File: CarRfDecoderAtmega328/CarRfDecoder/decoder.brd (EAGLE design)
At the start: 98.7 x 80 mm, 52 parts, among them T1 BC847, T2 BC847, T3 IRLML6402, U2 RFM69CW, U3 MCP73831, U4 ATMEGA328P, U6 MIC5219 3.3V, Y1 16MHZ

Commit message: bug fixes and better board routing
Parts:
- removed SS: (no value), wirepad:SMD1,27-2,54
- moved AUX3 17.3 mm to (15.7, 0.91)
- moved AUX4 17.3 mm to (17.6, 0.93)
- moved AUX2 17.3 mm to (13.8, 0.92)
- moved AUX1 17.3 mm to (12.0, 0.94)
- moved R9 10.7 mm to (13.3, 3.55), turned to 180 degrees
- moved SI 9.75 mm to (18.7, 17.5)
- moved SCK 7.94 mm to (16.8, 17.5)
- moved SER_V+ 6.53 mm to (10.2, 0.92)
- moved SER_DTR 6.33 mm to (8.40, 0.92)
- moved C1 6.19 mm to (5.92, 0.83)
- moved R1 5.87 mm to (3.02, 0.74)
- moved LIGHT 3.41 mm to (11.5, 17.4)
- moved SER_TX 3.35 mm to (23.8, 0.91)
- moved SER_RX 3.33 mm to (25.6, 0.90)
- moved GND 2.41 mm to (28.3, 2.72), turned to 90 degrees
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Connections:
- removed net AX1: R9.1, U4.25
- removed net AX2: R9.2, U4.22
- removed net AX3: R9.3, U4.19
- removed net AX4: R9.4, U4.10
- removed net N$24: AUX4.1, R9.5
- new net A2: R9.4, U4.25
- new net A6: C4.1, R6.3, R6.4, U4.19
- new net A7: R4.1, R5.2, U4.22
- new net D6: R9.2, U4.10
- new net M: AUX1.1, R9.5
- net A1: now also U3.1; no longer R11.1
- net A3: now also R9.3; no longer C4.1, R6.3, R6.4
- net A5: now also R9.1; no longer R4.1, R5.2
- net D7: now also R11.1; no longer U3.1
- net N$21: now also AUX4.1; no longer AUX1.1
- net N$22: now also AUX3.1; no longer AUX2.1
- net N$23: now also AUX2.1; no longer AUX3.1
- net SS: no longer SS.1
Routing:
- net GND: track 108.4 -> 126.9 mm, vias 9 -> 8
- net A7: track 0.00 -> 18.0 mm, vias 0 -> 1
- net BAT+: track 68.7 -> 52.0 mm, vias 7 -> 8
- net D6: track 0.00 -> 15.7 mm, vias 0 -> 4
- net D7: track 25.4 -> 10.0 mm
- net A5: track 19.9 -> 5.30 mm, vias 2 -> 0
- net AX1: track 12.5 -> 0.00 mm, vias 2 -> 0
- net A3: track 16.9 -> 5.52 mm, vias 2 -> 0
- net A6: track 0.00 -> 9.77 mm, vias 0 -> 1
- net SS: track 22.0 -> 12.5 mm, vias 2 -> 1
- net N$24: track 8.73 -> 0.00 mm
- net BL: track 6.59 -> 15.2 mm, vias 2 -> 0
- net AX4: track 8.59 -> 0.00 mm
- net SCK: track 27.8 -> 19.8 mm, vias 2 -> 1
- net AX2: track 7.52 -> 0.00 mm
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
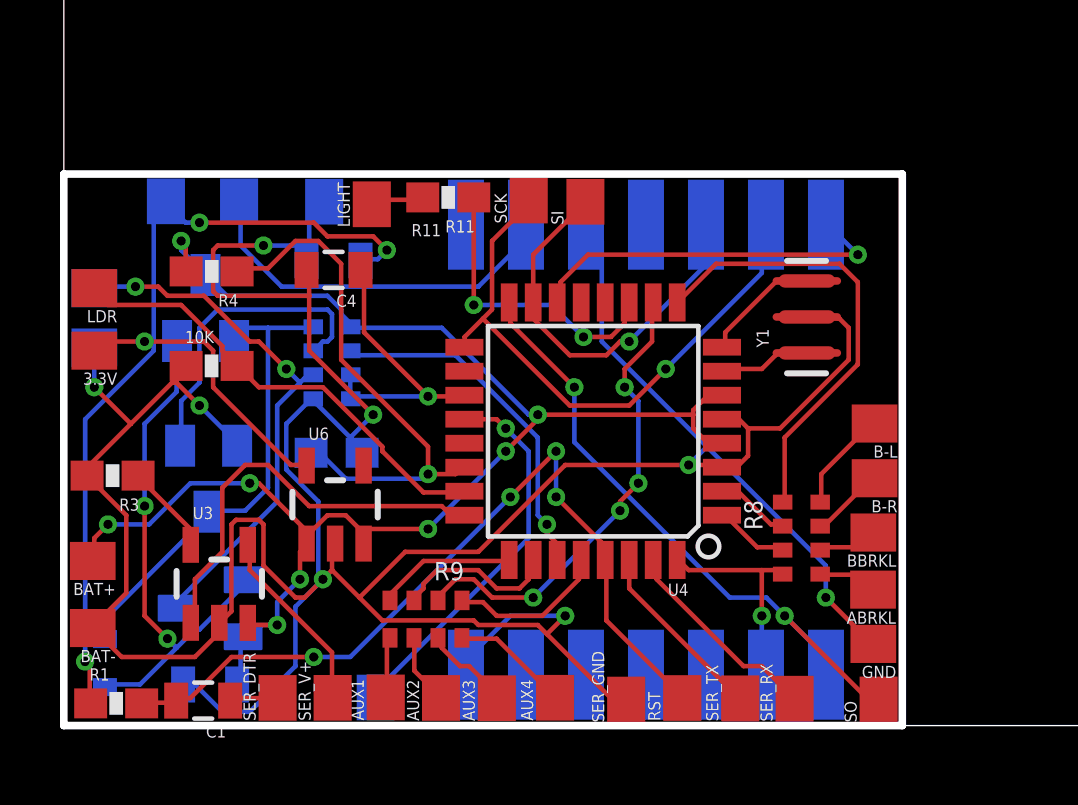
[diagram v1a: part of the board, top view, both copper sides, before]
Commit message: Fix light board. Fix carsystem board.
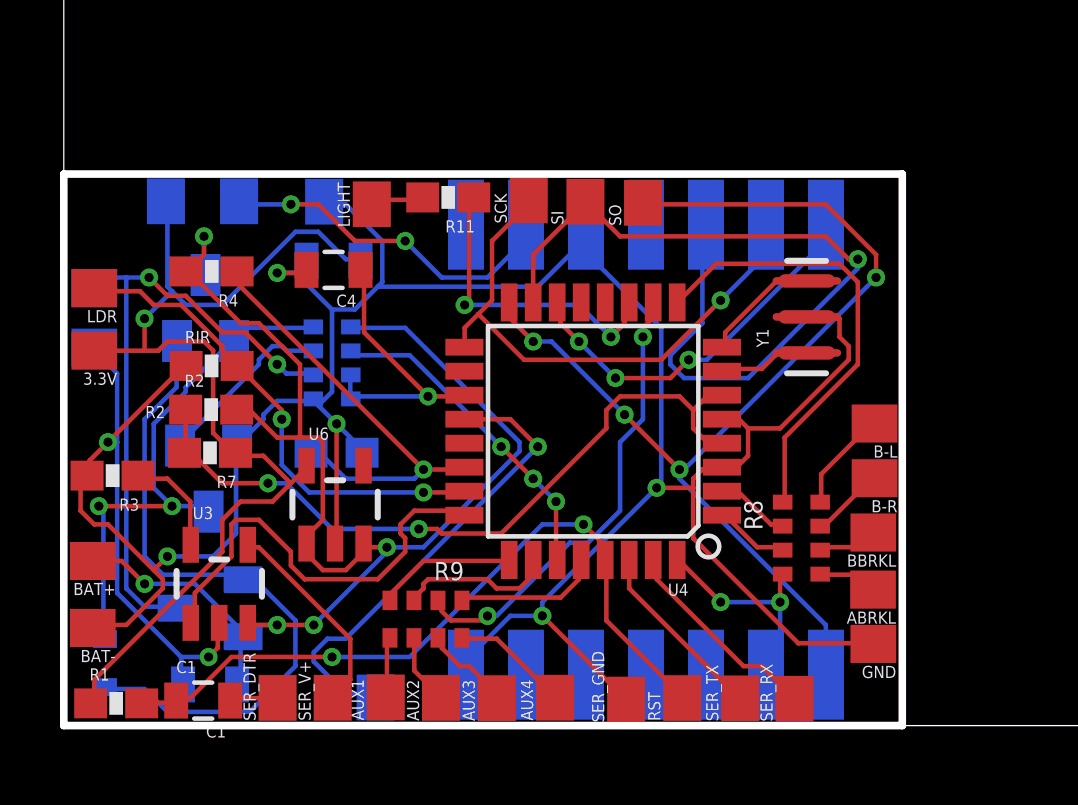
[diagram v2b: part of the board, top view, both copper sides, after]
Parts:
- added R2, R7: 0, SparkFun-Resistors:0603-RES
- moved SO 18.3 mm to (20.6, 17.4)
- renumbered 10K to RIR
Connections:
- new net N$6: R2.1, R7.2, U4.4, U4.6
- net BAT+: now also R2.2; no longer U4.4, U4.6
- net VCC: now also R7.1
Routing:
- net N$6: track 0.00 -> 24.9 mm, vias 0 -> 2
- net GND: track 126.9 -> 111.4 mm, vias 8 -> 7
- net MOSI: track 13.5 -> 27.4 mm
- net MISO: track 21.8 -> 35.6 mm, vias 2 -> 4
- net N$14: track 17.4 -> 22.4 mm, vias 2 -> 0
- net N$17: track 10.5 -> 6.01 mm
- net A7: track 18.0 -> 14.8 mm
- net N$15: track 18.0 -> 21.2 mm
- net AREF: track 13.0 -> 16.0 mm
- net N$5: track 27.3 -> 24.4 mm, vias 4 -> 2
- net BAT+: track 52.0 -> 49.5 mm, vias 8 -> 5
- net N$19: track 16.2 -> 18.0 mm, vias 0 -> 2
- net VCC: track 36.9 -> 35.2 mm, vias 4 -> 1
- net SCK: track 19.8 -> 18.5 mm
- net N$1: track 12.7 -> 11.6 mm, vias 0 -> 2
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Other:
- board text added: "C1"
- board text added: "R2"
- board text removed: "R11"

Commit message: CAM file for boards.
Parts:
- renumbered R2 to R_BAT, R7 to R_3.3V
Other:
- board text added: "R-BAT"
- board text removed: "R2"
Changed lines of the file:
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@@
 <layer number="20" name="Dimension" color="15" fill="1" visible="yes" active="yes"/>
 <layer number="21" name="tPlace" color="7" fill="1" visible="yes" active="yes"/>
-<layer number="22" name="bPlace" color="7" fill="1" visible="no" active="yes"/>
+<layer number="22" name="bPlace" color="7" fill="1" visible="yes" active="yes"/>
 <layer number="23" name="tOrigins" color="15" fill="1" visible="yes" active="yes"/>
 <layer number="24" name="bOrigins" color="15" fill="1" visible="yes" active="yes"/>
 <layer number="25" name="tNames" color="7" fill="1" visible="yes" active="yes"/>
-<layer number="26" name="bNames" color="7" fill="1" visible="no" active="yes"/>
+<layer number="26" name="bNames" color="7" fill="1" visible="yes" active="yes"/>
 <layer number="27" name="tValues" color="7" fill="1" visible="no" active="yes"/>
 <layer number="28" name="bValues" color="7" fill="1" visible="no" active="yes"/>
@@
 <layer number="116" name="Patch_BOT" color="9" fill="4" visible="no" active="yes"/>
 <layer number="121" name="_tsilk" color="7" fill="1" visible="yes" active="yes"/>
-<layer number="122" name="_bsilk" color="7" fill="1" visible="no" active="yes"/>
+<layer number="122" name="_bsilk" color="7" fill="1" visible="yes" active="yes"/>
 <layer number="123" name="tTestmark" color="7" fill="1" visible="no" active="yes"/>
 <layer number="124" name="bTestmark" color="7" fill="1" visible="no" active="yes"/>
@@
 <wire x1="29.21931875" y1="0" x2="1.27" y2="0" width="0.254" layer="20"/>
 <wire x1="1.27" y1="0" x2="1.27" y2="18.383696875" width="0.254" layer="20"/>
-<text x="13.6652" y="0.5588" size="0.4064" layer="122" rot="MR0">gnd</text>
+<text x="13.925321875" y="0.506771875" size="0.4064" layer="122" rot="MR0">gnd</text>
 <text x="17.526" y="17.2212" size="0.4064" layer="122" rot="MR90">3.3</text>
 <text x="27.2796" y="18.034" size="0.4064" layer="122" rot="MR180">hss</text>
@@
 <text x="23.4696" y="18.034" size="0.4064" layer="122" ratio="7" rot="MR180">si</text>
 <text x="19.6088" y="17.2212" size="0.4064" layer="122" rot="MR90">gnd</text>
-<text x="15.8496" y="0.3556" size="0.4064" layer="122" rot="MR90">rst</text>
+<text x="15.706534375" y="0.316575" size="0.4064" layer="122" rot="MR90">rst</text>
 <text x="5.0185" y="1.748625" size="0.4064" layer="121">C1</text>
-<text x="3.98438125" y="10.246528125" size="0.4064" layer="121">R2</text>
+<text x="2.959125" y="10.246528125" size="0.4064" layer="121">R-BAT</text>
 </plain>
 <attributes>
@@
 <element name="C1" library="SparkFun-Capacitors" package="0805" value="1uF" x="5.916221875" y="0.832240625" rot="R180"/>
 <element name="RST" library="wirepad" package="SMD1,27-2,54" value="" x="21.885759375" y="0.91805"/>
-<element name="R2" library="SparkFun-Resistors" package="0603-RES" value="0" x="6.18259375" y="10.53095625"/>
-<element name="R7" library="SparkFun-Resistors" package="0603-RES" value="0" x="6.143734375" y="9.091575" rot="R180"/>
+<element name="R_BAT" library="SparkFun-Resistors" package="0603-RES" value="0" x="6.18259375" y="10.53095625"/>
+<element name="R_3.3V" library="SparkFun-Resistors" package="0603-RES" value="0" x="6.143734375" y="9.091575" rot="R180"/>
 </elements>
 <signals>
@@
 <contactref element="VJ1" pad="1"/>
 <contactref element="C3" pad="2"/>
-<contactref element="R7" pad="1"/>
+<contactref element="R_3.3V" pad="1"/>
 <wire x1="10.668" y1="15.5448" x2="11.1252" y2="15.5448" width="0.1524" layer="16"/>
 <wire x1="9.7536" y1="16.4592" x2="10.668" y2="15.5448" width="0.1524" layer="16"/>
@@
 <contactref element="T3" pad="2"/>
 <contactref element="T1" pad="3"/>
-<contactref element="R2" pad="2"/>
+<contactref element="R_BAT" pad="2"/>
 <wire x1="7.4676" y1="10.5156" x2="7.1628" y2="10.5156" width="0.1524" layer="1"/>
 <wire x1="8.382" y1="9.6012" x2="7.4676" y2="10.5156" width="0.1524" layer="1"/>
@@
 <contactref element="U4" pad="6"/>
 <contactref element="U4" pad="4"/>
-<contactref element="R2" pad="1"/>
-<contactref element="R7" pad="2"/>
+<contactref element="R_BAT" pad="1"/>
+<contactref element="R_3.3V" pad="2"/>
 <wire x1="5.334" y1="10.5156" x2="5.334" y2="9.144" width="0.1524" layer="1"/>
 <wire x1="5.334" y1="9.144" x2="5.293734375" y2="9.091575" width="0.1524" layer="1"/>

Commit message: small fixes for vcc.
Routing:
- net GND: track 111.4 -> 0.00 mm, vias 7 -> 0
- net BAT+: track 49.5 -> 0.00 mm, vias 5 -> 0
- net MISO: track 35.6 -> 0.00 mm, vias 4 -> 0
- net VCC: track 35.2 -> 0.00 mm, vias 1 -> 0
- net MOSI: track 27.4 -> 0.00 mm, vias 1 -> 0
- net N$6: track 24.9 -> 0.00 mm, vias 2 -> 0
- net N$5: track 24.4 -> 0.00 mm, vias 2 -> 0
- net N$14: track 22.4 -> 0.00 mm
- net N$15: track 21.2 -> 0.00 mm, vias 2 -> 0
- net SCK: track 18.5 -> 0.00 mm, vias 1 -> 0
- net N$19: track 18.0 -> 0.00 mm, vias 2 -> 0
- net A0: track 16.4 -> 0.00 mm, vias 2 -> 0
- net AREF: track 16.0 -> 0.00 mm, vias 1 -> 0
- net D6: track 15.4 -> 0.00 mm, vias 2 -> 0
- net BL: track 15.2 -> 0.00 mm
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
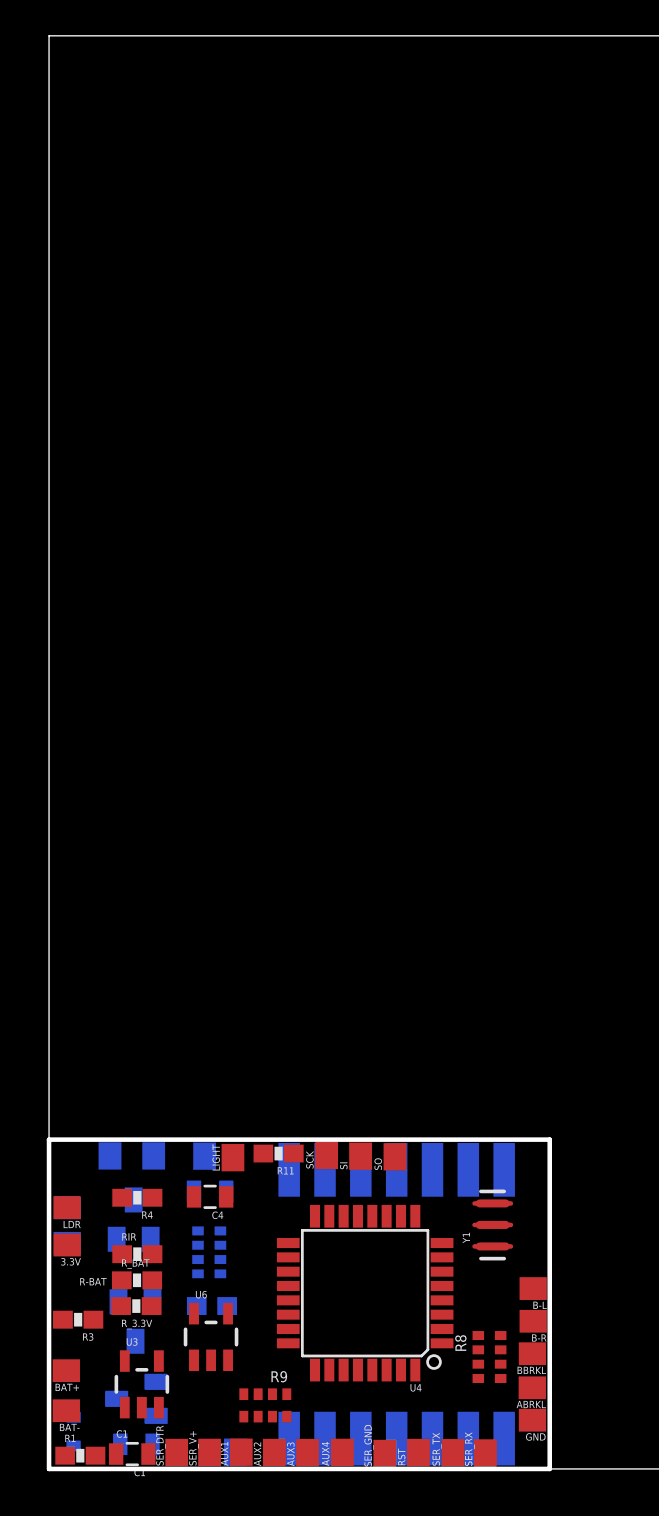
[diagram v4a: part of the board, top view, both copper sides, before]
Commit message: Change the pin to H-bridge to allow reverse control of the motor using A5
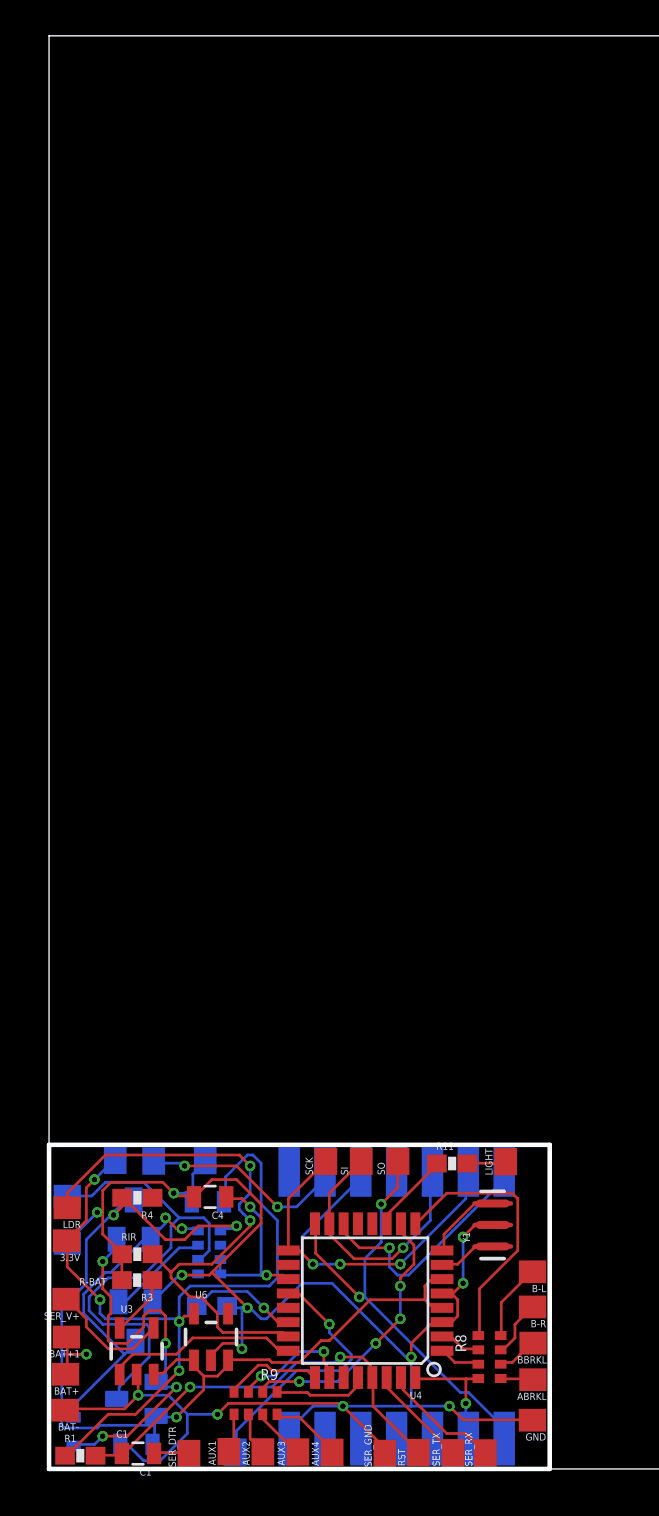
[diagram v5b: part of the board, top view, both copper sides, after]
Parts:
- removed R_3.3V, R_BAT: 0, SparkFun-Resistors:0603-RES
- added BAT+1: (no value), wirepad:SMD1,27-2,54
- moved LIGHT 15.2 mm to (26.8, 17.2)
- moved SER_V+ 11.7 mm to (2.22, 9.47), turned to 90 degrees
- moved R11 9.70 mm to (23.8, 17.0), turned to 0 degrees
- moved R3 3.97 mm to (6.19, 10.5)
- moved U3 1.87 mm to (6.16, 6.57)
- moved B-L 0.94 mm to (28.3, 11.0)
- moved B-R 0.80 mm to (28.3, 9.04)
- moved AUX1 0.69 mm to (11.3, 0.97)
- moved SER_DTR 0.69 mm to (9.08, 0.86)
- moved MOTOR 0.65 mm to (2.29, 15.2)
- moved AUX2 0.64 mm to (13.2, 0.95)
- moved C3 0.60 mm to (10.1, 14.9)
- moved BBRKL 0.59 mm to (28.3, 7.02)
- moved AUX4 0.57 mm to (17.1, 0.93)
- moved R9 0.56 mm to (12.8, 3.67)
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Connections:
- removed net N$6: R_3.3V.2, R_BAT.1, U4.4, U4.6
- net BAT+: now also BAT+1.1, U4.4, U4.6; no longer R_BAT.2
- net VCC: no longer R_3.3V.1
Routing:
- net GND: track 0.00 -> 116.7 mm, vias 0 -> 12
- net BAT+: track 0.00 -> 61.7 mm, vias 0 -> 4
- net VCC: track 0.00 -> 45.3 mm, vias 0 -> 4
- net A0: track 0.00 -> 31.6 mm, vias 0 -> 2
- net N$15: track 0.00 -> 28.4 mm
- net MISO: track 0.00 -> 25.1 mm, vias 0 -> 2
- net N$5: track 0.00 -> 23.8 mm, vias 0 -> 2
- net N$14: track 0.00 -> 23.7 mm, vias 0 -> 4
- net SCK: track 0.00 -> 19.3 mm, vias 0 -> 3
- net N$19: track 0.00 -> 18.7 mm, vias 0 -> 2
- net D6: track 0.00 -> 15.4 mm, vias 0 -> 4
- net BL: track 0.00 -> 15.1 mm
- net MOSI: track 0.00 -> 14.8 mm, vias 0 -> 1
- net AREF: track 0.00 -> 14.8 mm, vias 0 -> 1
- net SS: track 0.00 -> 13.8 mm, vias 0 -> 1
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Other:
- outline, holes or cut-outs redrawn

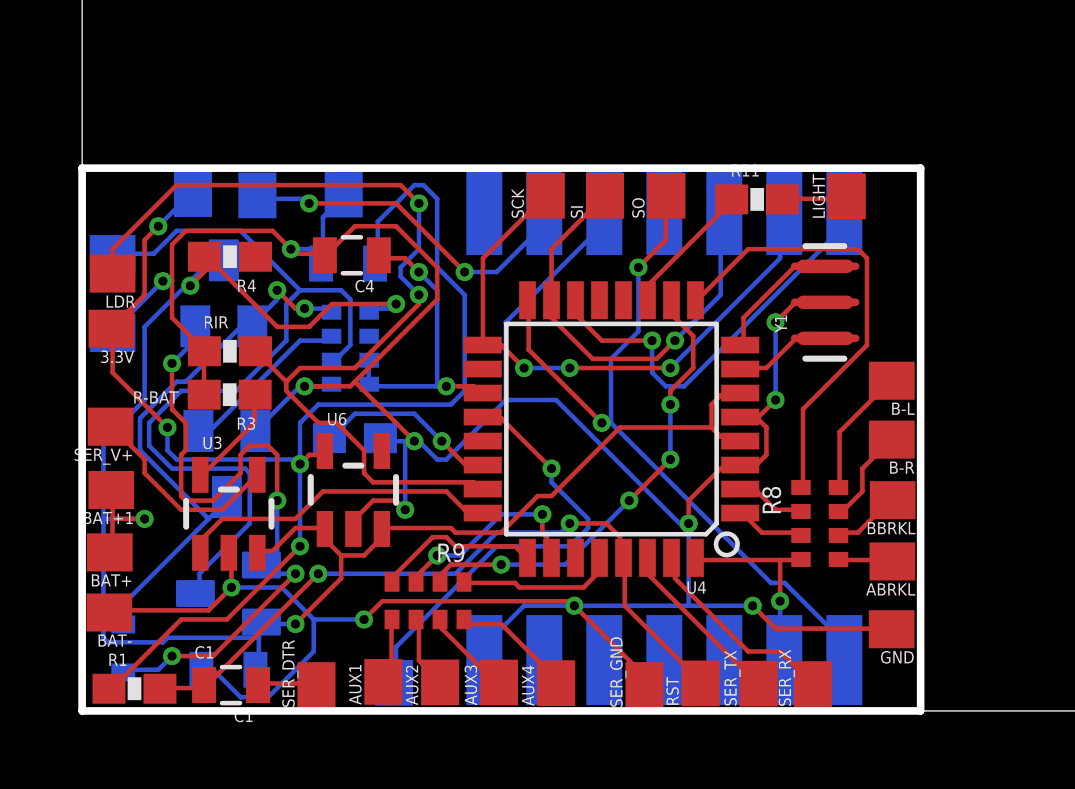
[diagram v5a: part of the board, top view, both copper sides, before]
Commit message: New layout for RFM69HC
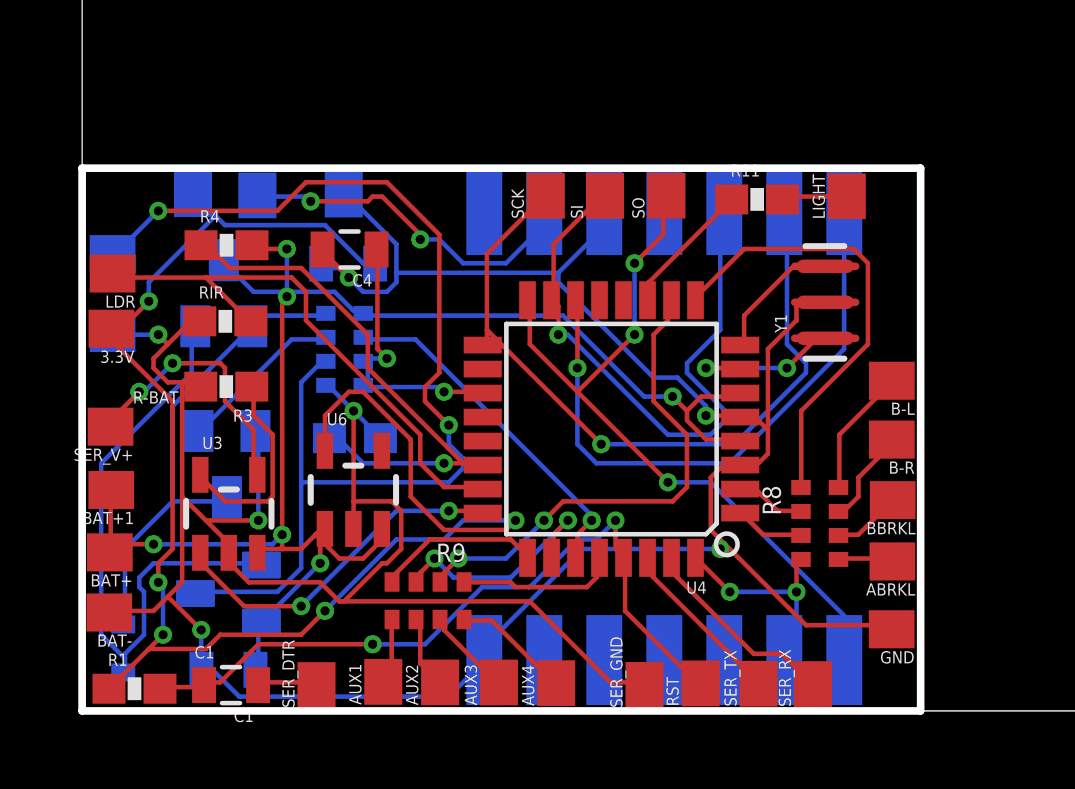
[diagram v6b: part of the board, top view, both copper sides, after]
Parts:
- removed 2.56V: (no value), wirepad:SMD1,27-2,54
- moved RIR 1.01 mm to (6.04, 13.0)
- moved R4 0.40 mm to (6.08, 15.5), turned to 0 degrees
- moved R3 0.29 mm to (6.08, 10.8)
- moved C4 0.21 mm to (10.2, 15.4)
- moved R6 0.20 mm to (10.0, 12.1)
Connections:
- net AREF: no longer 2.56V.1
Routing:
- net AREF: track 14.8 -> 0.00 mm, vias 1 -> 0
- net A0: track 31.6 -> 18.6 mm, vias 2 -> 0
- net A7: track 6.14 -> 18.0 mm
- net A4: track 0.00 -> 11.7 mm, vias 0 -> 1
- net N$15: track 28.4 -> 37.9 mm, vias 0 -> 2
- net BAT+: track 61.7 -> 53.0 mm, vias 4 -> 6
- net SS: track 13.8 -> 20.2 mm
- net VCC: track 45.3 -> 51.5 mm, vias 4 -> 5
- net MOSI: track 14.8 -> 20.8 mm
- net SCK: track 19.3 -> 24.9 mm, vias 3 -> 1
- net N$11: track 3.46 -> 6.85 mm
- net N$2: track 2.25 -> 5.53 mm, vias 0 -> 2
- net N$14: track 23.7 -> 20.5 mm, vias 4 -> 0
- net N$19: track 18.7 -> 16.3 mm, vias 2 -> 0
- net N$9: track 6.78 -> 9.08 mm, vias 0 -> 2
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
